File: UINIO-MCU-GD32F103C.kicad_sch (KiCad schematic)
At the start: 1 part

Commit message: Complete schematic drawing.
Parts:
- added C1, C3, C4, C6, C7, C9: 0.1uF, Capacitor_SMD:C_0603_1608Metric, symbol Device:C
- added C10, C11: 10pF, Capacitor_SMD:C_0603_1608Metric, symbol Device:C
- added C12, C8: 20pF, Capacitor_SMD:C_0603_1608Metric, symbol Device:C
- added C2, C5: 1uF, Capacitor_SMD:C_0603_1608Metric, symbol Device:C
- added D1: LED_Red, LED_SMD:LED_0603_1608Metric, symbol Device:LED
- added J1, J2: Conn_01x24_Male, Connector_PinHeader_2.54mm:PinHeader_1x24_P2.54mm_Vertical, symbol Connector:Conn_01x24_Male
- added J3: Conn_01x04_Male, Connector_PinHeader_2.54mm:PinHeader_1x04_P2.54mm_Vertical, symbol Connector:Conn_01x04_Male
- added L1: 1KΩ 100Mhz, Inductor_SMD:L_0603_1608Metric, symbol Device:L
- added R1: 2K, Resistor_SMD:R_0603_1608Metric, symbol Device:R
- added R10, R5, R6, R8, R9: 10K, Resistor_SMD:R_0603_1608Metric, symbol Device:R
- added R2, R3: 50R, Resistor_SMD:R_0603_1608Metric, symbol Device:R
- added R4: 1.5K, Resistor_SMD:R_0603_1608Metric, symbol Device:R
- added R7: 1M, Resistor_SMD:R_0603_1608Metric, symbol Device:R
- added SW1: BOOT1, Uinio:KEY-SMD_4P-L4.2-W3.4-P2.15-LS4.7, symbol Uinio:Key_YTS_A016S_1
- added SW2: NRST, Uinio:KEY-SMD_4P-L4.2-W3.4-P2.15-LS4.7, symbol Uinio:Key_YTS_A016S_1
- added SW3: BOOT0, Uinio:KEY-SMD_4P-L4.2-W3.4-P2.15-LS4.7, symbol Uinio:Key_YTS_A016S_1
- added U1: ME6211C33M5G-N, Uinio:SOT-23-5_L3.0-W1.7-P0.95-LS2.8-BR, symbol Uinio:ME6211
- added USB1: USB_Type_C_16Pin, Uinio:USB-C-SMD_TYPEC-304J-BCP16, symbol Uinio:USB_Type_C_16Pin
- added Y1: 32.768KHz, Uinio:CRYSTAL-FC135-32.768, symbol Uinio:Crystal-32.768KHz
- added Y2: 8MHz, Crystal:Crystal_SMD_3225-4Pin_3.2x2.5mm, symbol Device:Crystal_GND24
- gave numbers to parts that had none: 1
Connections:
- net VBAT: now reaches U2.1 (VBAT)
- net VBAT: now also J2.15 (Pin_15)
- net PA0: now reaches U2.10 (PA0_WAKEUP)
- net PA0: now also J2.22 (Pin_22)
- net PA1: now reaches U2.11 (PA1)
- net PA1: now also J2.23 (Pin_23)
- net PA2: now reaches U2.12 (PA2)
- net PA2: now also J2.24 (Pin_24)
- net PA3: now reaches U2.13 (PA3)
- net PA3: now also J1.24 (Pin_24)
- net PA4: now reaches U2.14 (PA4)
- net PA4: now also J1.23 (Pin_23)
- net PA5: now reaches U2.15 (PA5)
- net PA5: now also J1.22 (Pin_22)
- net PA6: now reaches U2.16 (PA6)
- net PA6: now also J1.21 (Pin_21)
- net PA7: now reaches U2.17 (PA7)
- net PA7: now also J1.20 (Pin_20)
- net PB0: now reaches U2.18 (PB0)
- net PB0: now also J1.19 (Pin_19)
- net PB1: now reaches U2.19 (PB1)
- net PB1: now also J1.18 (Pin_18)
- net PC13: now reaches U2.2 (PC13_TAMPER_RTC)
- net PC13: now also J2.16 (Pin_16)
- net PB2/BOOT1: now reaches U2.20 (PB2)
- net PB2/BOOT1: now also C1.2, J1.17 (Pin_17), R5.1
- net PB10: now reaches U2.21 (PB10)
- net PB10: now also J1.16 (Pin_16)
- net PB11: now reaches U2.22 (PB11)
- net PB11: now also J1.15 (Pin_15)
- net GND: now reaches U2.23 (VSS_1)
- net GND: now also U2.35 (VSS_2), U2.47 (VSS_3), C1.1, C10.1, C11.1, C12.1, C2.1, C3.1, C4.1, C5.1, C6.1, C7.1, C8.1, C9.2, D1.1 (K), J1.1 (Pin_1), J1.13 (Pin_13), J2.1 (Pin_1), J2.13 (Pin_13), J2.18 (Pin_18), J2.21 (Pin_21), J3.1 (Pin_1), L1.1, R10.2, R5.2, R8.1, SW1.1, SW1.2, SW2.3, SW2.4, SW3.1, SW3.2, U1.2 (Vss), USB1.13 (GND), USB1.14 (GND), USB1.15 (GND), USB1.16 (GND), USB1.A1B12 (GND), USB1.B1A12 (GND)
- net VDD_3.3V: now reaches U2.24 (VDD_1)
- net VDD_3.3V: now also U2.36 (VDD_2), U2.48 (VDD_3), U2.9 (VDDA), C3.2, C4.2, C5.2, C6.2, J1.14 (Pin_14), J1.2 (Pin_2), J2.14 (Pin_14), J2.17 (Pin_17), J2.20 (Pin_20), J3.4 (Pin_4), R4.1, R6.1, R9.2, SW1.3, SW1.4, SW3.3, SW3.4, U1.5 (Vout)
- net PB12: now reaches U2.25 (PB12)
- net PB12: now also J1.12 (Pin_12)
- net PB13: now reaches U2.26 (PB13)
- net PB13: now also J1.11 (Pin_11)
- net PB14: now reaches U2.27 (PB14)
- net PB14: now also J1.10 (Pin_10)
- net PB15: now reaches U2.28 (PB15)
- net PB15: now also J1.9 (Pin_9)
- net PA8: now reaches U2.29 (PA8)
- net PA8: now also J1.8 (Pin_8)
- net at U2.3 (PC14_OSC32_IN): now also C10.2, Y1.2 (GND)
- net PA9: now reaches U2.30 (PA9)
- net PA9: now also J1.7 (Pin_7)
- net PA10: now reaches U2.31 (PA10)
- net PA10: now also J1.6 (Pin_6)
- net PA11: now reaches U2.32 (PA11)
- net PA11: now also J1.5 (Pin_5), R3.1
- net PA12: now reaches U2.33 (PA12)
- net PA12: now also J1.4 (Pin_4), R2.1, R4.2
- net PA13/SWDIO: now reaches U2.34 (PA13)
- net PA13/SWDIO: now also J1.3 (Pin_3), J3.3 (Pin_3), R9.1
- net PA14/SWCLK: now reaches U2.37 (PA14)
- net PA14/SWCLK: now also J2.3 (Pin_3), J3.2 (Pin_2), R8.2
- net PA15: now reaches U2.38 (PA15)
- net PA15: now also J2.4 (Pin_4)
- net PB3: now reaches U2.39 (PB3)
- net PB3: now also J2.5 (Pin_5)
- net at U2.4 (PC15_OSC32_OUT): now also C11.2, Y1.1
- net PB4: now reaches U2.40 (PB4)
- net PB4: now also J2.6 (Pin_6)
- net PB5: now reaches U2.41 (PB5)
- net PB5: now also J2.7 (Pin_7)
- net PB6: now reaches U2.42 (PB6)
- net PB6: now also J2.8 (Pin_8)
- net PB7: now reaches U2.43 (PB7)
- net PB7: now also J2.9 (Pin_9)
- net BOOT0: now reaches U2.44 (BOOT0)
- net BOOT0: now also C7.2, J2.10 (Pin_10), R10.1
- net PB8: now reaches U2.45 (PB8)
- net PB8: now also J2.11 (Pin_11)
- net PB9: now reaches U2.46 (PB9)
- net PB9: now also J2.12 (Pin_12)
- net at U2.5 (PD0_OSC_IN): now also R7.1, Y2.3
- net at U2.6 (PD1_OSC_OUT): now also R7.2, Y2.1
- net NRST: now reaches U2.7 (NRST)
- net NRST: now also C9.1, J2.19 (Pin_19), R6.2, SW2.1, SW2.2
- net at U2.8 (VSSA): now also L1.2
- new net: D1.2 (A), R1.1
- new net: C12.2, Y2.2
- new net: C8.2, Y2.4
- new net USB_Data+: R2.2, USB1.A6 (DP1), USB1.B6 (DP2)
- new net USB_Data-: R3.2, USB1.A7 (DN1), USB1.B7 (DN2)
- new net VDD_5V: C2.2, J2.2 (Pin_2), R1.2, U1.1 (Vin), U1.3 (CE), USB1.A4B9 (VBUS), USB1.B4A9 (VBUS)
- no-connect marks 0 -> 5
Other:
- note added: "2.54mm 排针"
- note added: "3.3V 线性稳压电路"
- note added: "GD32F103Cxxx 最小系统"
- note added: "SWD 调试接口"
- note added: "USB Type-C 接口电路"
- moved on the sheet: U2

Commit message: Finish PCB Layout.
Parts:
- C1, C10, C11, C12, C2, C3, C4, C5, C6, C7, C8, C9: footprint Capacitor_SMD:C_0603_1608Metric -> Capacitor_SMD:C_0402_1005Metric
- R1, R10, R2, R3, R4, R5, R6, R7, R8, R9: footprint Resistor_SMD:R_0603_1608Metric -> Resistor_SMD:R_0402_1005Metric
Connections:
- net VDD_3.3V: now also R1.2
- net VDD_5V: no longer R1.2
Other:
- moved on the sheet: C2, C5, C9, D1, R1, SW2, U1

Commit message: Prepare version 2.0.0.
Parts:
- removed J1, J2: Conn_01x24_Male, Connector_PinHeader_2.54mm:PinHeader_1x24_P2.54mm_Vertical, symbol Connector:Conn_01x24_Male
- removed J3: Conn_01x04_Male, Connector_PinHeader_2.54mm:PinHeader_1x04_P2.54mm_Vertical, symbol Connector:Conn_01x04_Male
- added J1, J2: Conn_01x24_Pin, Connector_PinHeader_2.54mm:PinHeader_1x24_P2.54mm_Vertical, symbol Connector:Conn_01x24_Pin
- added J3: Conn_01x04_Pin, Connector_PinHeader_2.54mm:PinHeader_1x04_P2.54mm_Vertical, symbol Connector:Conn_01x04_Pin
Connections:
- net BOOT0: now also J2.10 (Pin_10)
- net GND: now also J1.1 (Pin_1), J1.13 (Pin_13), J2.1 (Pin_1), J2.13 (Pin_13), J2.18 (Pin_18), J2.21 (Pin_21), J3.1 (Pin_1)
- net NRST: now also J2.19 (Pin_19)
- net PA0: now also J2.22 (Pin_22)
- net PA1: now also J2.23 (Pin_23)
- net PA10: now also J1.6 (Pin_6)
- net PA11: now also J1.5 (Pin_5)
- net PA12: now also J1.4 (Pin_4)
- net PA13/SWDIO: now also J1.3 (Pin_3), J3.3 (Pin_3)
- net PA14/SWCLK: now also J2.3 (Pin_3), J3.2 (Pin_2)
- net PA15: now also J2.4 (Pin_4)
- net PA2: now also J2.24 (Pin_24)
- net PA3: now also J1.24 (Pin_24)
- net PA4: now also J1.23 (Pin_23)
- net PA5: now also J1.22 (Pin_22)
- net PA6: now also J1.21 (Pin_21)
- net PA7: now also J1.20 (Pin_20)
- net PA8: now also J1.8 (Pin_8)
- net PA9: now also J1.7 (Pin_7)
- net PB0: now also J1.19 (Pin_19)
- net PB1: now also J1.18 (Pin_18)
- net PB10: now also J1.16 (Pin_16)
- net PB11: now also J1.15 (Pin_15)
- net PB12: now also J1.12 (Pin_12)
- net PB13: now also J1.11 (Pin_11)
- net PB14: now also J1.10 (Pin_10)
- net PB15: now also J1.9 (Pin_9)
- net PB2/BOOT1: now also J1.17 (Pin_17)
- net PB3: now also J2.5 (Pin_5)
- net PB4: now also J2.6 (Pin_6)
- net PB5: now also J2.7 (Pin_7)
- net PB6: now also J2.8 (Pin_8)
- net PB7: now also J2.9 (Pin_9)
- net PB8: now also J2.11 (Pin_11)
- net PB9: now also J2.12 (Pin_12)
- net PC13: now also J2.16 (Pin_16)
- net VBAT: now also J2.15 (Pin_15)
- net VDD_3.3V: now also J1.14 (Pin_14), J1.2 (Pin_2), J2.14 (Pin_14), J2.17 (Pin_17), J2.20 (Pin_20), J3.4 (Pin_4)
- net VDD_5V: now also J2.2 (Pin_2)
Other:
- moved on the sheet: C12, R7

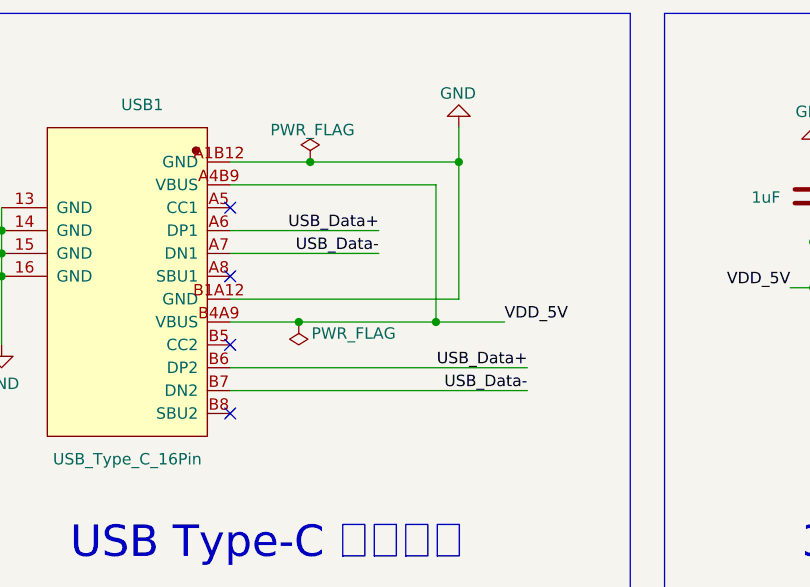
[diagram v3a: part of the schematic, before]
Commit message: Release UINIO-MCU-GD32F103C version 3.0.0.
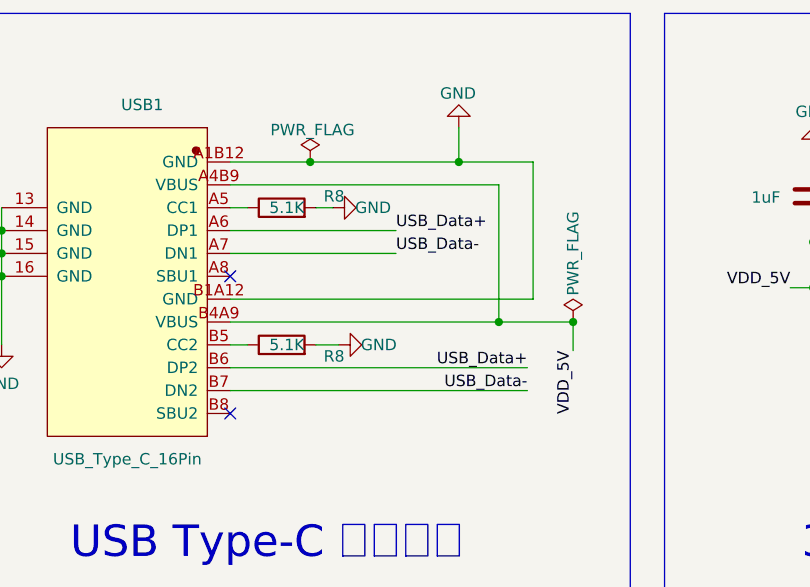
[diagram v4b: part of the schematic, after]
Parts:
- added R8 (x2): 5.1K, Resistor_SMD:R_0402_1005Metric, symbol Device:R
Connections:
- net GND: now also R8.2, R8.2
- net at USB1.A5 (CC1): now also R8.1
- net at USB1.B5 (CC2): now also R8.1
- no-connect marks 5 -> 3
